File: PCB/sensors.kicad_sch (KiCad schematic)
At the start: 15 parts, among them U5 BME280, U7 OPA340NA

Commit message: Finished PCB routing and added reference designators
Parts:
- renumbered C21 to C23, C22 to C24, C30 to C25, C31 to C26, C26 to C27, D7 to D6, D8 to D7, R21 to R18, R12 to R19, R13 to R20, R15 to R21, R17 to R22, U5 to U8
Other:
- moved on the sheet: C27, D6, D7, R21, R22, S1

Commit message: Final touches to PCB
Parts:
- added C27, C29: 100n, Capacitor_SMD:C_0402_1005Metric, symbol Device:C
- added R19, R24: 500, Resistor_SMD:R_0402_1005Metric, symbol Device:R
- added TP3, TP4: TestPoint, TestPoint:TestPoint_Pad_D1.0mm, symbol Connector:TestPoint
- C25: value 1u -> 500n
- renumbered C27 to C28, R19 to R20, R20 to R21, R21 to R22, R22 to R23
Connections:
- net GND: now also C27.2, C29.2
- net Light level: now also C27.1, R19.2, TP3.1; no longer C25.2, R18.2, U7.1
- net Soil_cap: now also C29.1, R24.1, TP4.1; no longer C28.2, D7.1 (K), R23.2
- new net: C28.2, D7.1 (K), R23.2, R24.2
- new net V_out: C25.2, R18.2, R19.1, U7.1
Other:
- note added: "Additional current limit and low pass noise filter"
- note added: "Transimpedance amplifier Vout/Iin = -Rf/(RfCfs + 1) -3dB cut off at 9.65Hz for chosen component values."
- note removed: "Transimpedance amplifier Vout/Iin = -Rf/(RfCfs + 1)"
- moved on the sheet: C23, C24, C25, C26, C28, D6, D7, R18, R20, R21, R22, R23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

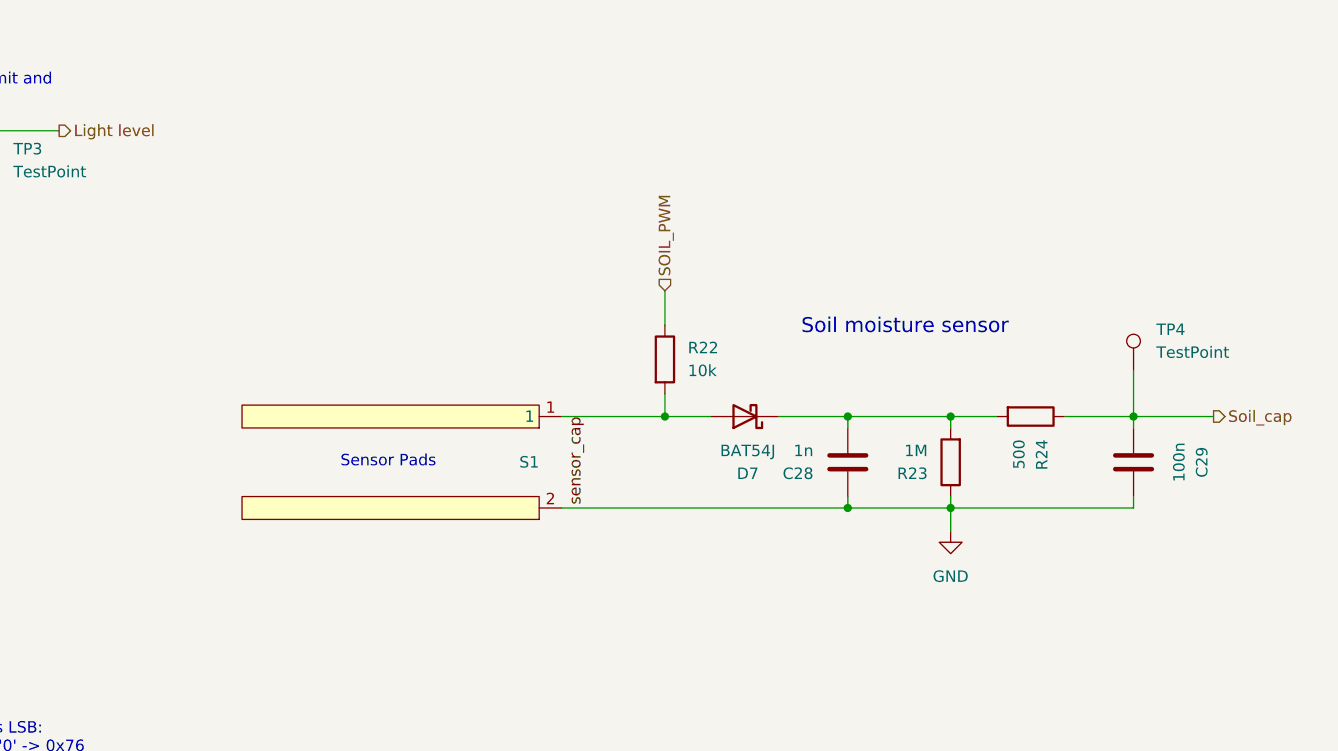
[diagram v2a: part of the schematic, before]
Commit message: ESD protection and Boost UVLO
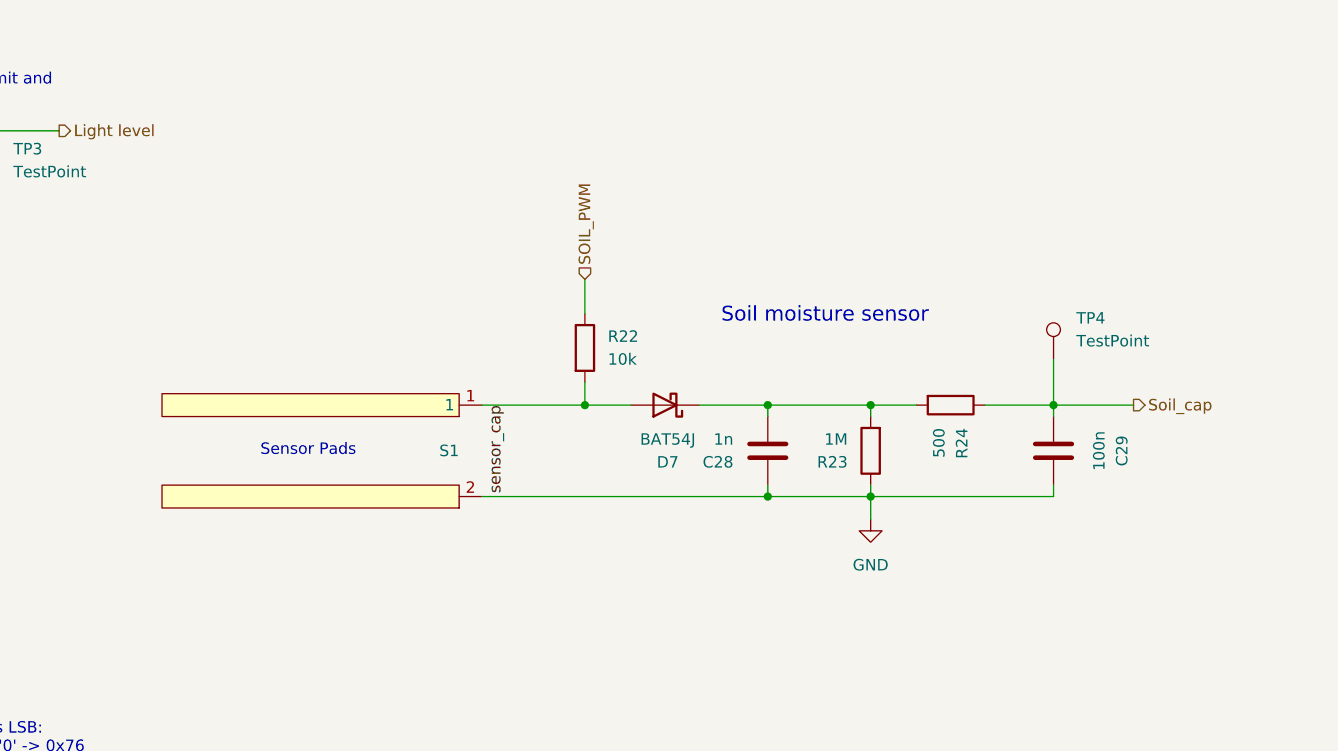
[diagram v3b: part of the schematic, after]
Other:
- moved on the sheet: C28, C29, D7, R22, R23, R24, S1, TP4

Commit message: Production files
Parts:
- removed R20, R21: 0, Resistor_SMD:R_0603_1608Metric, symbol Device:R
- C25: value 500n -> 220n; footprint Capacitor_SMD:C_0603_1608Metric -> Capacitor_SMD:C_0402_1005Metric
- R19: value 500 -> 510
- R22: renamed from R24; value 500 -> 510
- renumbered D7 to D10, D6 to D9, R22 to R20, R23 to R21
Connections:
- net GND: now also U8.5 (SDO)
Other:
- note added: "Transimpedance amplifier Vout/Iin = -Rf/(RfCfs + 1) -3dB cut off at 21.9Hz for chosen component values."
- note removed: "Transimpedance amplifier Vout/Iin = -Rf/(RfCfs + 1) -3dB cut off at 9.65Hz for chosen component values."
